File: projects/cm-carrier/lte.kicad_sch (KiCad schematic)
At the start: 22 parts, among them J6 EC25-J Mini PCIe, J7 nanoSIM, Q1 2N7002, Q2 2N7002, U9 TPD4E05U06DQA

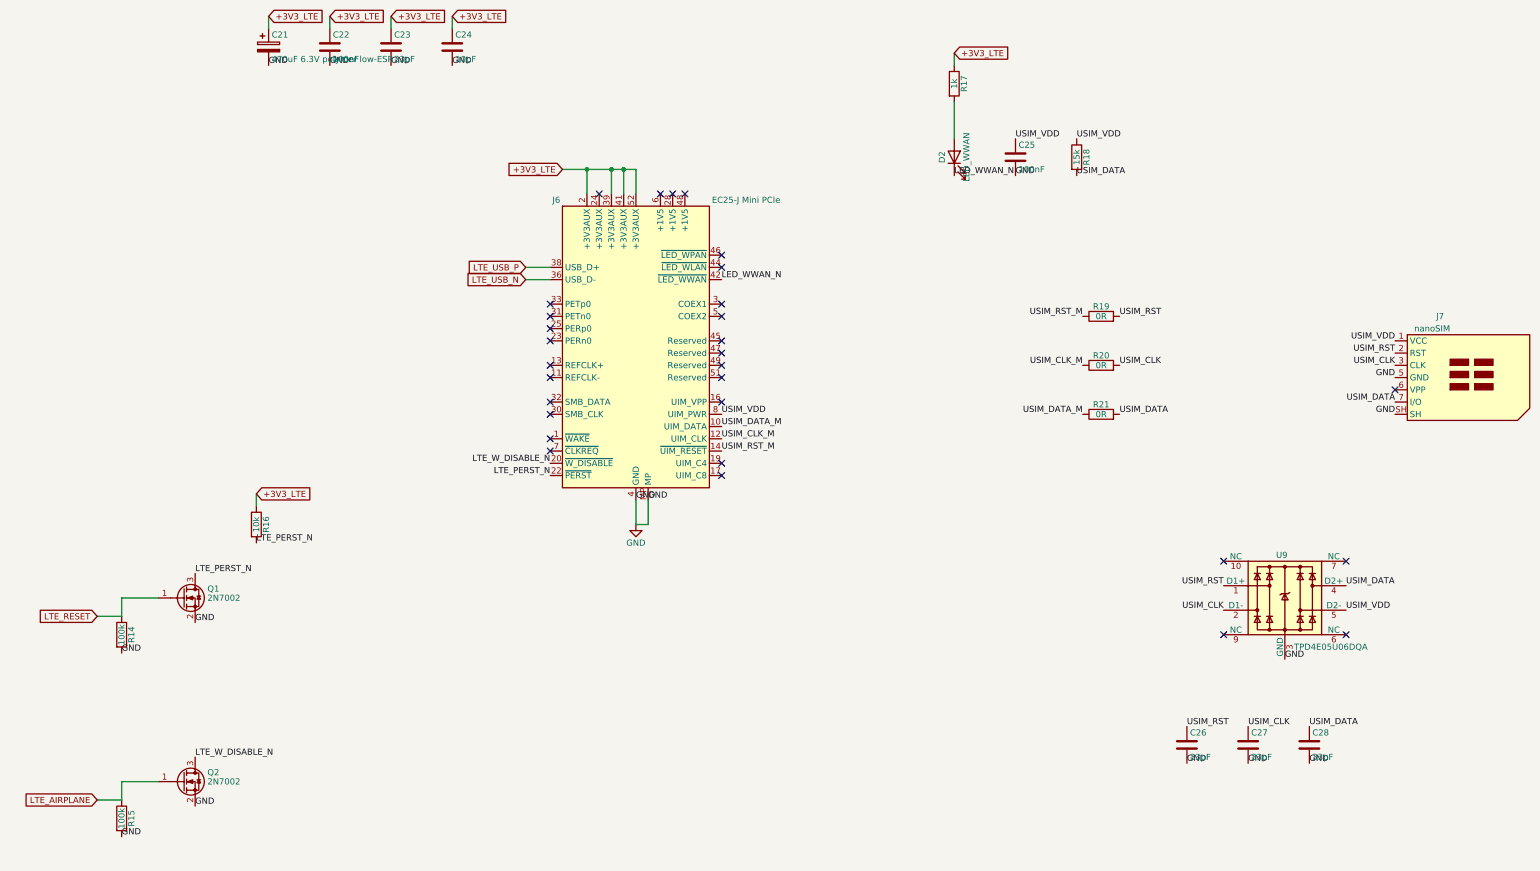
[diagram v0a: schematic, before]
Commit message: cm-carrier: schematic readability cleanup (no netlist change)
Co-Authored-By: Claude Opus 5.5 <noreply@anthropic.com>
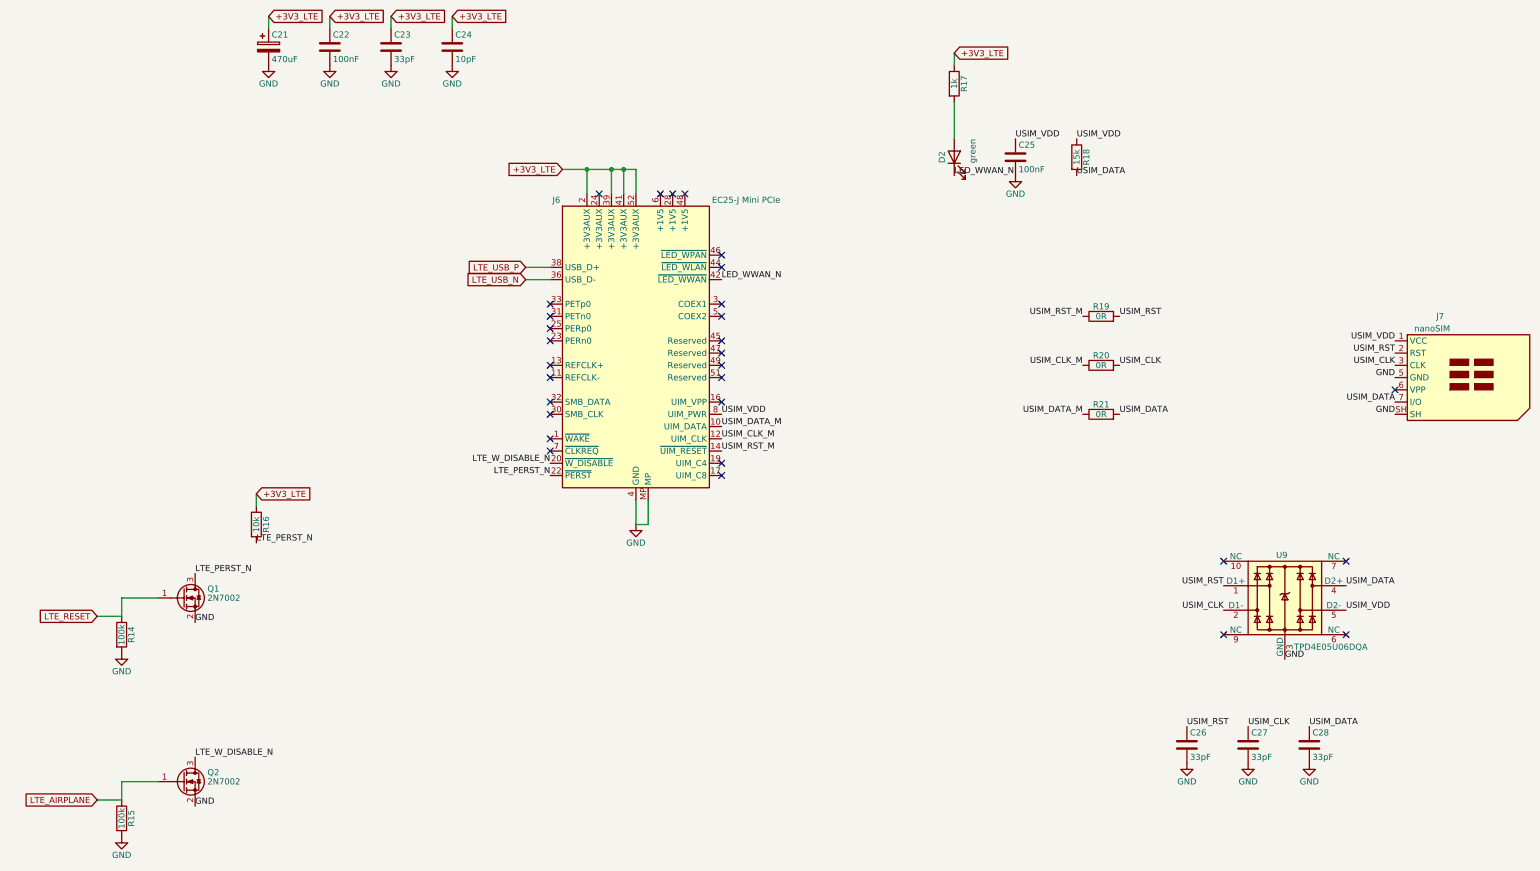
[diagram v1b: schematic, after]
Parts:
- C21: value 470uF 6.3V polymer low-ESR -> 470uF
- D2: value LED_WWAN -> green
